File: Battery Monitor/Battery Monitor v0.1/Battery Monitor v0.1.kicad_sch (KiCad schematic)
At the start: 31 parts, among them J1 XT60 M (Vertical), J2 Raspberry Pi 5, Q1 SUD50P10-43L, U1 15V~40V -> 12V 30A, U2 6~25V -> 5V 8A

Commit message: Began adding footprints & datasheets
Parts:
- C1: footprint (none) -> Capacitor_THT:CP_Radial_D16.0mm_P7.50mm
- C4: footprint (none) -> Capacitor_THT:CP_Radial_D10.0mm_P5.00mm
- C5, C6: footprint (none) -> Capacitor_SMD:C_1206_3216Metric_Pad1.33x1.80mm_HandSolder
- D1: footprint (none) -> Diode_SMD:Nexperia_CFP3_SOD-123W
- D2, D3, D4, D5: footprint (none) -> LED_SMD:LED_0805_2012Metric_Pad1.15x1.40mm_HandSolder
- D7: footprint (none) -> Diode_SMD:D_SMC_Handsoldering
- F1: footprint (none) -> Fuse:FuseHolder_Blade_ATO_Littelfuse_FLR_178.6165
- F2, F3: footprint (none) -> Fuse:Fuse_1206_3216Metric
- FB1, FB2: footprint (none) -> Inductor_SMD:L_0805_2012Metric_Pad1.05x1.20mm_HandSolder
- H1, H2, H3, H4: footprint (none) -> MountingHole:MountingHole_3.2mm_M3_DIN965_Pad_TopBottom
- J1: footprint (none) -> Connector_AMASS:AMASS_XT60PW-M_1x02_P7.20mm_Horizontal
- Q1: footprint (none) -> Package_TO_SOT_SMD:TO-252-2
- R1, R3, R4, R5: footprint (none) -> Resistor_SMD:R_0805_2012Metric_Pad1.20x1.40mm_HandSolder
- R2: value 1k 0603 -> 1k 0805; footprint (none) -> Resistor_SMD:R_0805_2012Metric_Pad1.20x1.40mm_HandSolder
- U1: footprint Library:Buck Converter -> Library:Buck_Converter_74x74mm
- U2: footprint Library:Buck Converter -> Library:Buck_Converter_30x20mm
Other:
- note added: "Note to self: See if there are any simple 5.1V alternatives"
- note added: "Warning: No back-power protection. Use an isolator if connecting directly to Pi with USB. Remote recommended."
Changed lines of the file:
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@@
 		)
 	)
+	(text "Warning: No back-power protection. Use an isolator if connecting directly to Pi with USB. Remote recommended."
+		(exclude_from_sim no)
+		(at 92.202 100.838 0)
+		(effects
+			(font
+				(size 1.27 1.27)
+				(color 194 0 0 1)
+			)
+			(justify left)
+		)
+	)
+	(text "Note to self: See if there are any simple 5.1V alternatives"
+		(exclude_from_sim no)
+		(at 19.812 146.304 0)
+		(effects
+			(font
+				(size 1.27 1.27)
+				(color 194 0 0 1)
+			)
+			(justify left)
+		)
+	)
 	(junction
 		(at 101.6 134.62)
@@
 			)
 		)
-		(property "Footprint" ""
+		(property "Footprint" "MountingHole:MountingHole_3.2mm_M3_DIN965_Pad_TopBottom"
 			(at 260.35 152.4 0)
 			(hide yes)
@@
 			)
 		)
-		(property "Footprint" ""
+		(property "Footprint" "LED_SMD:LED_0805_2012Metric_Pad1.15x1.40mm_HandSolder"
 			(at 182.88 152.4 0)
 			(hide yes)
@@
 			)
 		)
-		(property "Footprint" ""
+		(property "Footprint" "Connector_AMASS:AMASS_XT60PW-M_1x02_P7.20mm_Horizontal"
 			(at 24.13 35.56 0)
 			(hide yes)
@@
 			)
 		)
-		(property "Footprint" "Library:Buck Converter"
+		(property "Footprint" "Library:Buck_Converter_74x74mm"
 			(at 49.53 92.71 0)
 			(hide yes)
@@
 			)
 		)
-		(property "Footprint" ""
+		(property "Footprint" "Capacitor_THT:CP_Radial_D16.0mm_P7.50mm"
 			(at 68.2752 43.18 0)
 			(hide yes)
@@
 			)
 		)
-		(property "Footprint" ""
+		(property "Footprint" "Inductor_SMD:L_0805_2012Metric_Pad1.05x1.20mm_HandSolder"
 			(at 245.11 38.608 90)
 			(hide yes)
@@
 			)
 		)
-		(property "Footprint" ""
+		(property "Footprint" "Fuse:FuseHolder_Blade_ATO_Littelfuse_FLR_178.6165"
 			(at 36.83 37.338 90)
 			(hide yes)
@@
 			)
 		)
-		(property "Datasheet" ""
+		(property "Datasheet" "https://www.littelfuse.com/assetdocs/ato-flr-datasheet?assetguid=bef6771d-7ae2-4b18-8f55-8cde6402100a"
 			(at 36.83 35.56 0)
 			(hide yes)
@@
 			)
 		)
-		(property "Footprint" ""
+		(property "Footprint" "Resistor_SMD:R_0805_2012Metric_Pad1.20x1.40mm_HandSolder"
 			(at 46.482 46.99 90)
 			(hide yes)
@@
 			)
 		)
-		(property "Footprint" ""
+		(property "Footprint" "Capacitor_THT:CP_Radial_D10.0mm_P5.00mm"
 			(at 40.3352 134.62 0)
 			(hide yes)
@@
 			)
 		)
-		(property "Footprint" ""
+		(property "Footprint" "LED_SMD:LED_0805_2012Metric_Pad1.15x1.40mm_HandSolder"
 			(at 182.88 132.08 0)
 			(hide yes)
@@
 			)
 		)
-		(property "Footprint" ""
+		(property "Footprint" "MountingHole:MountingHole_3.2mm_M3_DIN965_Pad_TopBottom"
 			(at 267.97 152.4 0)
 			(hide yes)
@@
 			)
 		)
-		(property "Footprint" ""
+		(property "Footprint" "MountingHole:MountingHole_3.2mm_M3_DIN965_Pad_TopBottom"
 			(at 252.73 152.4 0)
 			(hide yes)
@@
 			)
 		)
-		(property "Footprint" ""
+		(property "Footprint" "LED_SMD:LED_0805_2012Metric_Pad1.15x1.40mm_HandSolder"
 			(at 182.88 142.24 0)
 			(hide yes)
@@
 			)
 		)
-		(property "Footprint" ""
+		(property "Footprint" "LED_SMD:LED_0805_2012Metric_Pad1.15x1.40mm_HandSolder"
 			(at 182.88 121.92 0)
 			(hide yes)
@@
 			)
 		)
-		(property "Footprint" ""
+		(property "Footprint" "MountingHole:MountingHole_3.2mm_M3_DIN965_Pad_TopBottom"
 			(at 275.59 152.4 0)
 			(hide yes)
@@
 			)
 		)
-		(property "Footprint" ""
+		(property "Footprint" "Inductor_SMD:L_0805_2012Metric_Pad1.05x1.20mm_HandSolder"
 			(at 181.61 37.338 90)
 			(hide yes)
@@
 			)
 		)
-		(property "Footprint" "Library:Buck Converter"
+		(property "Footprint" "Library:Buck_Converter_30x20mm"
 			(at 54.61 137.16 0)
 			(hide yes)
@@
 			)
 		)
-		(property "Datasheet" "https://item.taobao.com/item.htm?id=535067252604&last_time=1775529713&mi_id=0000S7qq-__YN9-Xo7hKoFTzNDnUlEApIXqSNfFMFeaf8do&scm=1007.13982.82927.0&spm=tbpc.mytb_footmark.item.goods&upStreamPrice=1568&skuId=3193614541540"
+		(property "Datasheet" "https://item.taobao.com/item.htm?id=535067252604&last_time=1775529713&mi_id=0000S7qq-__YN9-https://item.taobao.com/item.htm?id=959630171148&mi_id=0000m_zm79GKZcsIwMOyhy4vHlEAIzmYNFW1XXsxhAtvo4Q&spm=tbpc.mytb_itemcollect.item.goods&upStreamPrice=880"
 			(at 54.61 139.7 0)
 			(hide yes)
@@
 			)
 		)
-		(property "Footprint" ""
+		(property "Footprint" "Resistor_SMD:R_0805_2012Metric_Pad1.20x1.40mm_HandSolder"
 			(at 193.04 154.178 90)
 			(hide yes)
@@
 			)
 		)
-		(property "Footprint" ""
+		(property "Footprint" "Diode_SMD:Nexperia_CFP3_SOD-123W"
 			(at 55.88 39.37 0)
 			(hide yes)
@@
 			)
 		)
-		(property "Datasheet" ""
+		(property "Datasheet" "https://www.mouser.hk/ProductDetail/Nexperia/BZT52-C15X?qs=%252BEew9%252B0nqrCP9M4nxqpvsw%3D%3D"
 			(at 55.88 39.37 0)
 			(hide yes)
@@
 			)
 		)
-		(property "Footprint" ""
+		(property "Footprint" "Fuse:Fuse_1206_3216Metric"
 			(at 199.39 34.29 0)
 			(hide yes)
@@
 			)
 		)
-		(property "Footprint" ""
+		(property "Footprint" "Capacitor_SMD:C_1206_3216Metric_Pad1.33x1.80mm_HandSolder"
 			(at 102.5652 134.62 0)
 			(hide yes)
@@
 			)
 		)
-		(property "Footprint" ""
+		(property "Footprint" "Fuse:Fuse_1206_3216Metric"
 			(at 256.54 38.1 0)
 			(hide yes)
@@
 			)
 		)
-		(property "Footprint" ""
+		(property "Footprint" "Diode_SMD:D_SMC_Handsoldering"
 			(at 30.48 125.73 0)
 			(hide yes)
@@
 			)
 		)
-		(property "Value" "1k 0603"
+		(property "Value" "1k 0805"
 			(at 193.04 118.11 90)
 			(show_name no)
@@
 			)
 		)
-		(property "Footprint" ""
+		(property "Footprint" "Resistor_SMD:R_0805_2012Metric_Pad1.20x1.40mm_HandSolder"
 			(at 193.04 123.698 90)
 			(hide yes)
@@
 			)
 		)
-		(property "Footprint" ""
+		(property "Footprint" "Package_TO_SOT_SMD:TO-252-2"
 			(at 45.72 33.02 0)
 			(hide yes)
@@
 			)
 		)
-		(property "Datasheet" ""
+		(property "Datasheet" "https://www.vishay.com/docs/62504/sud50p10-43l-ge3.pdf"
 			(at 48.26 38.1 0)
 			(hide yes)
@@
 			)
 		)
-		(property "Footprint" ""
+		(property "Footprint" "Resistor_SMD:R_0805_2012Metric_Pad1.20x1.40mm_HandSolder"
 			(at 193.04 144.018 90)
 			(hide yes)
@@
 			)
 		)
-		(property "Footprint" ""
+		(property "Footprint" "Resistor_SMD:R_0805_2012Metric_Pad1.20x1.40mm_HandSolder"
 			(at 193.04 133.858 90)
 			(hide yes)
@@
 			)
 		)
-		(property "Footprint" ""
+		(property "Footprint" "Capacitor_SMD:C_1206_3216Metric_Pad1.33x1.80mm_HandSolder"
 			(at 86.0552 134.62 0)
 			(hide yes)

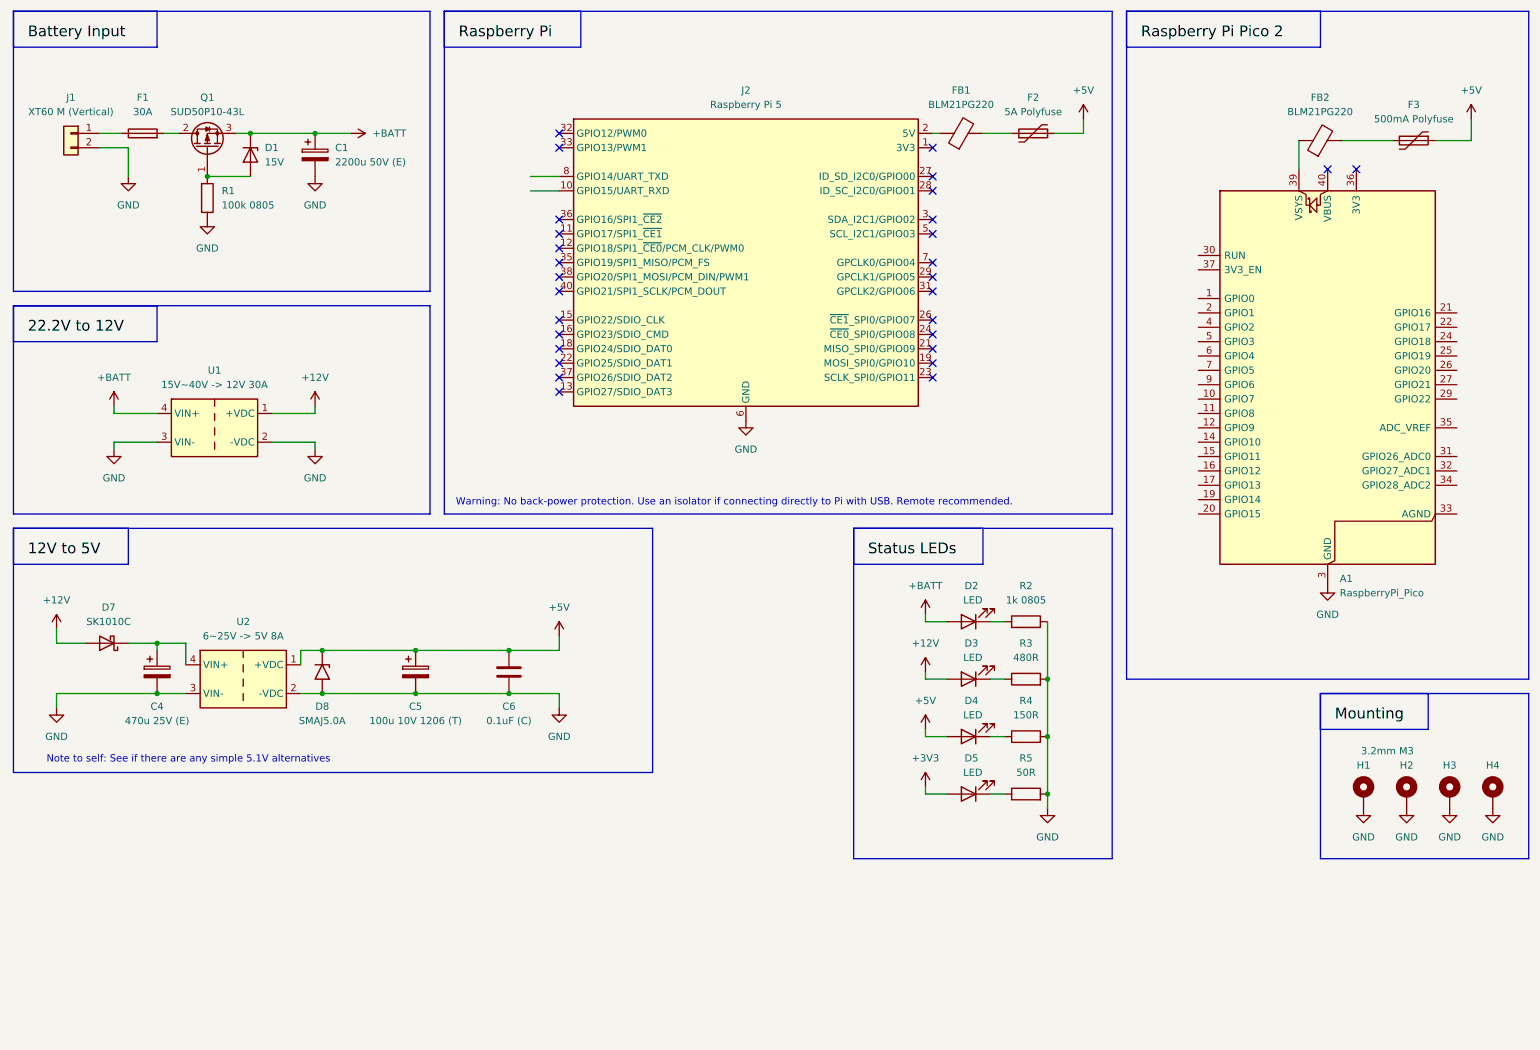
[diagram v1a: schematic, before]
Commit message: Finished design. TODO: Servo actually 7.4V. Needs fix
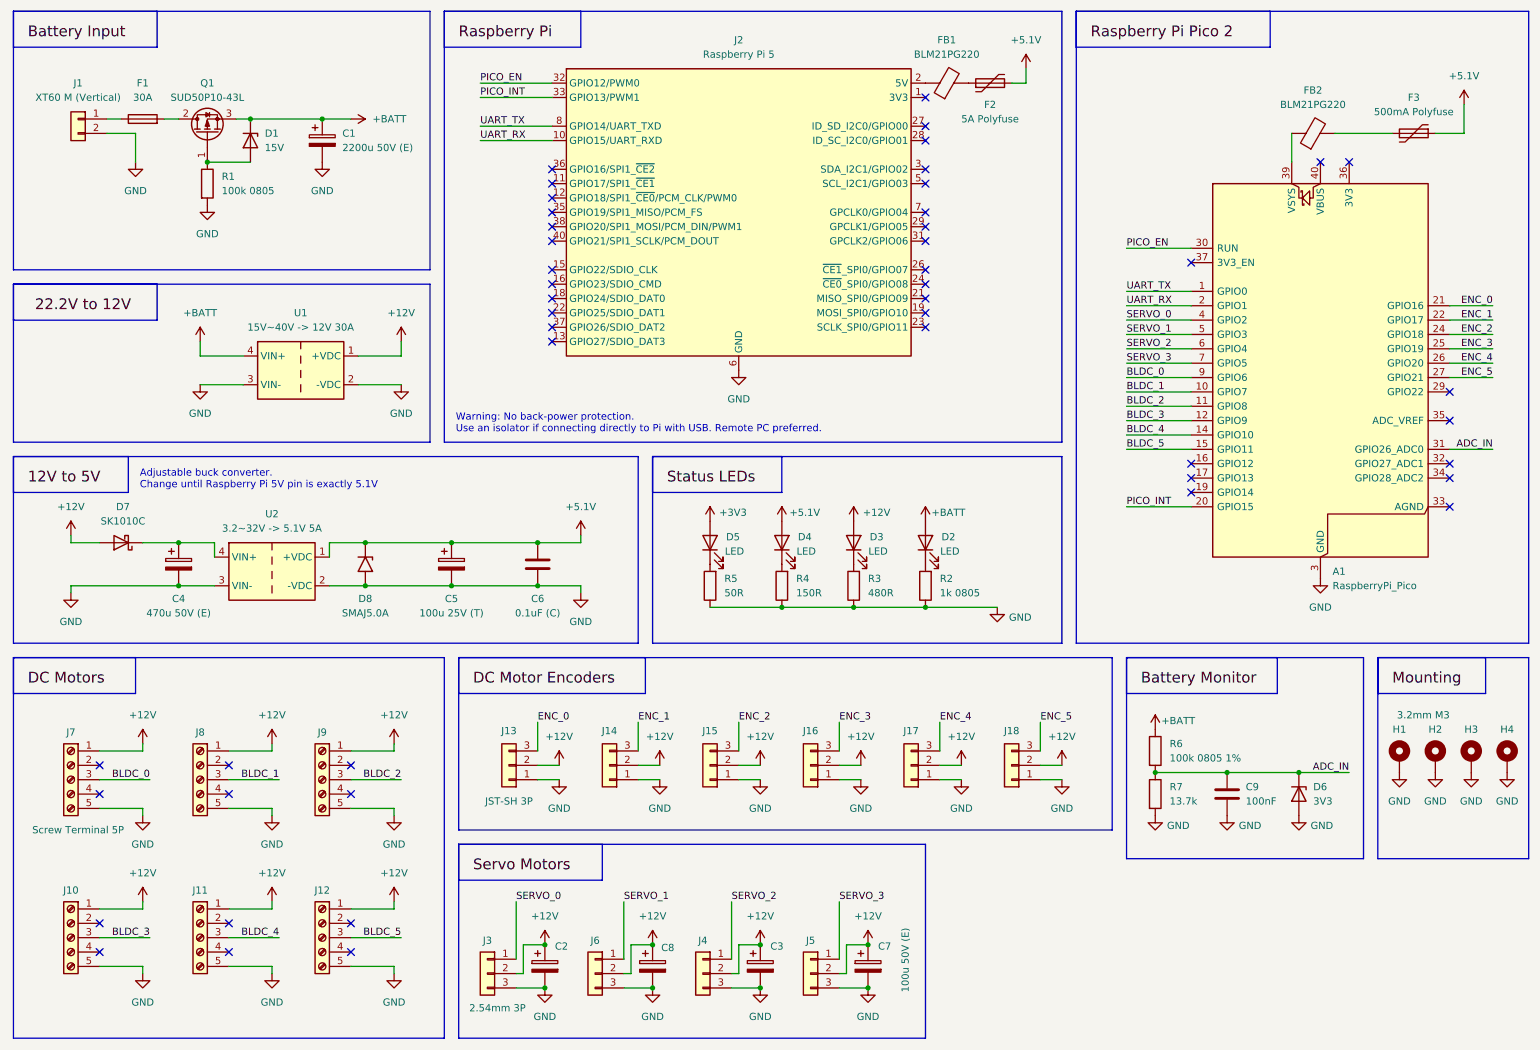
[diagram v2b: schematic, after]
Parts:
- added C2, C3, C7, C8: 100u 50V (E), Capacitor_THT:CP_Radial_D16.0mm_P7.50mm, symbol Device:C_Polarized
- added C9: 100nF, Capacitor_SMD:C_1206_3216Metric_Pad1.33x1.80mm_HandSolder, symbol Device:C
- added D6: 3V3, Diode_SMD:Nexperia_CFP3_SOD-123W, symbol Device:D_Zener
- added J10, J11, J12, J7, J8, J9: Screw Terminal 5P, symbol Connector:Screw_Terminal_01x05
- added J13, J14, J15, J16, J17, J18: JST-SH 3P, symbol Connector_Generic:Conn_01x03
- added J3, J4, J5, J6: 2.54mm 3P, symbol Connector_Generic:Conn_01x03
- added R6: 100k 0805 1%, Resistor_SMD:R_0805_2012Metric_Pad1.20x1.40mm_HandSolder, symbol Device:R
- added R7: 13.7k, Resistor_SMD:R_0805_2012Metric_Pad1.20x1.40mm_HandSolder, symbol Device:R
- C4: value 470u 25V (E) -> 470u 50V (E)
- C5: value 100u 10V 1206 (T) -> 100u 25V (T)
- U2: value 6~25V -> 5V 8A -> 3.2~32V -> 5.1V 5A; footprint Library:Buck_Converter_30x20mm -> Library:Buck_Converter_44x22mm
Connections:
- net +12V: now also C2.1, C3.1, C7.1, C8.1, J10.1 (Pin_1), J11.1 (Pin_1), J12.1 (Pin_1), J13.2 (Pin_2), J14.2 (Pin_2), J15.2 (Pin_2), J16.2 (Pin_2), J17.2 (Pin_2), J18.2 (Pin_2), J3.2 (Pin_2), J4.2 (Pin_2), J5.2 (Pin_2), J6.2 (Pin_2), J7.1 (Pin_1), J8.1 (Pin_1), J9.1 (Pin_1)
- net +BATT: now also R6.1
- net GND: now also R2.1, R3.1, R4.1, R5.1, C2.2, C3.2, C7.2, C8.2, C9.2, D6.2 (A), J10.5 (Pin_5), J11.5 (Pin_5), J12.5 (Pin_5), J13.1 (Pin_1), J14.1 (Pin_1), J15.1 (Pin_1), J16.1 (Pin_1), J17.1 (Pin_1), J18.1 (Pin_1), J3.3 (Pin_3), J4.3 (Pin_3), J5.3 (Pin_3), J6.3 (Pin_3), J7.5 (Pin_5), J8.5 (Pin_5), J9.5 (Pin_5), R7.2; no longer R2.2, R3.2, R4.2, R5.2
- net at D5.1 (K): now also R5.2; no longer R5.1
- net UART_RX: now reaches J2.10 (GPIO15/UART_RXD)
- net UART_RX: now also A1.2 (GPIO1)
- net PICO_EN: now reaches J2.32 (GPIO12/PWM0)
- net PICO_EN: now also A1.30 (RUN)
- net PICO_INT: now reaches J2.33 (GPIO13/PWM1)
- net PICO_INT: now also A1.20 (GPIO15)
- net UART_TX: now reaches J2.8 (GPIO14/UART_TXD)
- net UART_TX: now also A1.1 (GPIO0)
- net at D3.1 (K): now also R3.2; no longer R3.1
- net BLDC_1: now reaches A1.10 (GPIO7)
- net BLDC_1: now also J8.3 (Pin_3)
- net BLDC_2: now reaches A1.11 (GPIO8)
- net BLDC_2: now also J9.3 (Pin_3)
- net BLDC_3: now reaches A1.12 (GPIO9)
- net BLDC_3: now also J10.3 (Pin_3)
- net BLDC_4: now reaches A1.14 (GPIO10)
- net BLDC_4: now also J11.3 (Pin_3)
- net BLDC_5: now reaches A1.15 (GPIO11)
- net BLDC_5: now also J12.3 (Pin_3)
- net ENC_0: now reaches A1.21 (GPIO16)
- net ENC_0: now also J13.3 (Pin_3)
- net ENC_1: now reaches A1.22 (GPIO17)
- net ENC_1: now also J14.3 (Pin_3)
- net ENC_2: now reaches A1.24 (GPIO18)
- net ENC_2: now also J15.3 (Pin_3)
- net ENC_3: now reaches A1.25 (GPIO19)
- net ENC_3: now also J16.3 (Pin_3)
- net ENC_4: now reaches A1.26 (GPIO20)
- net ENC_4: now also J17.3 (Pin_3)
- net ENC_5: now reaches A1.27 (GPIO21)
- net ENC_5: now also J18.3 (Pin_3)
- net ADC_IN: now reaches A1.31 (GPIO26_ADC0)
- net ADC_IN: now also C9.1, D6.1 (K), R6.2, R7.1
- net SERVO_0: now reaches A1.4 (GPIO2)
- net SERVO_0: now also J3.1 (Pin_1)
- net SERVO_1: now reaches A1.5 (GPIO3)
- net SERVO_1: now also J6.1 (Pin_1)
- net SERVO_2: now reaches A1.6 (GPIO4)
- net SERVO_2: now also J4.1 (Pin_1)
- net SERVO_3: now reaches A1.7 (GPIO5)
- net SERVO_3: now also J5.1 (Pin_1)
- net BLDC_0: now reaches A1.9 (GPIO6)
- net BLDC_0: now also J7.3 (Pin_3)
- net at D4.1 (K): now also R4.2; no longer R4.1
- net at D2.1 (K): now also R2.2; no longer R2.1
- net +5V renamed +5.1V
- no-connect marks 29 -> 48
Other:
- note added: "Adjustable buck converter. Change until Raspberry Pi 5V pin is exactly 5.1V"
- note added: "Warning: No back-power protection. Use an isolator if connecting directly to Pi with USB. Remote PC preferred."
- note removed: "Note to self: See if there are any simple 5.1V alternatives"
- note removed: "Warning: No back-power protection. Use an isolator if connecting directly to Pi with USB. Remote recommended."
- moved on the sheet: A1, C1, C4, C5, C6, D1, D2, D3, D4, D5, D7, D8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
